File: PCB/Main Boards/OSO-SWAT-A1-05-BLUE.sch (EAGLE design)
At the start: 34 parts, among them J1 FH19C-9S-0.5SH_10_, U1 ATSAML22J18A-MUT, U2 MIC5365-3.3YC5-TR, X1 32.768

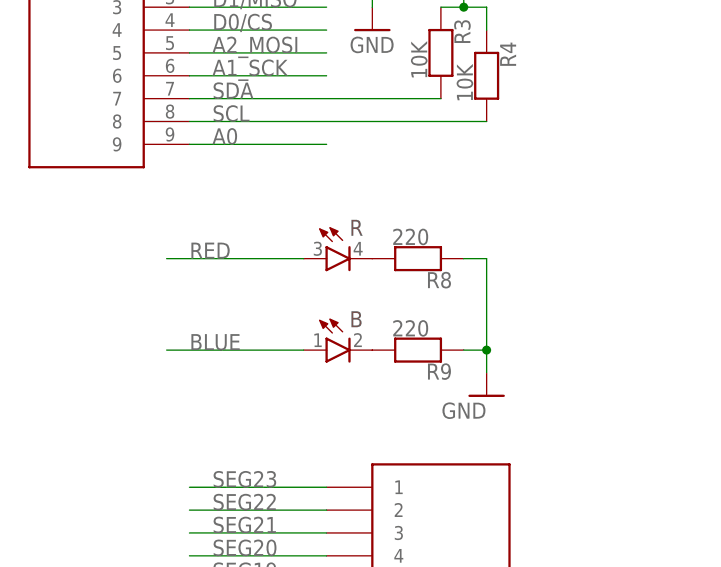
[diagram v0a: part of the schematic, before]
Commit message: fix LED resistor values
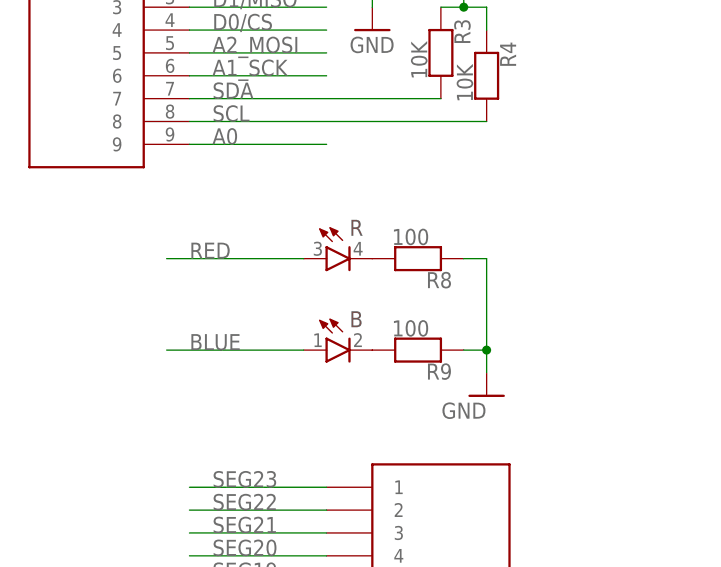
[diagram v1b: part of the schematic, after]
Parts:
- R8, R9: value 220 -> 100
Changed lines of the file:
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@@
 <part name="RESET" library="EVP-BB1AAB000" deviceset="EVP-BB1AAB000" device=""/>
 <part name="GND15" library="supply1" deviceset="GND" device=""/>
-<part name="R8" library="microbuilder" deviceset="RESISTOR" device="_0603MP" value="220"/>
-<part name="R9" library="microbuilder" deviceset="RESISTOR" device="_0603MP" value="220"/>
+<part name="R8" library="microbuilder" deviceset="RESISTOR" device="_0603MP" value="100"/>
+<part name="R9" library="microbuilder" deviceset="RESISTOR" device="_0603MP" value="100"/>
 <part name="R2" library="microbuilder" deviceset="RESISTOR" device="_0603MP" value="10K"/>
 <part name="SUPPLY5" library="SparkFun-PowerSymbols" deviceset="VCC" device=""/>
